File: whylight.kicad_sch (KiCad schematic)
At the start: 69 parts, among them J1 USB device, J2 External 5v, J3 External 5v, J4 I2C, J5 UART, J7 Ledstrip, U1 AG5405, U10 INA233, U11 L78L05_SOT89, U2 KPC357NT0ATLD, U3 ESP32-C6-WROOM-1, U4 Ra-01SH, U6 AP63203WU, U7 USBLC6-2P6, U8 74LVC1G125, U9 74LVC1G125

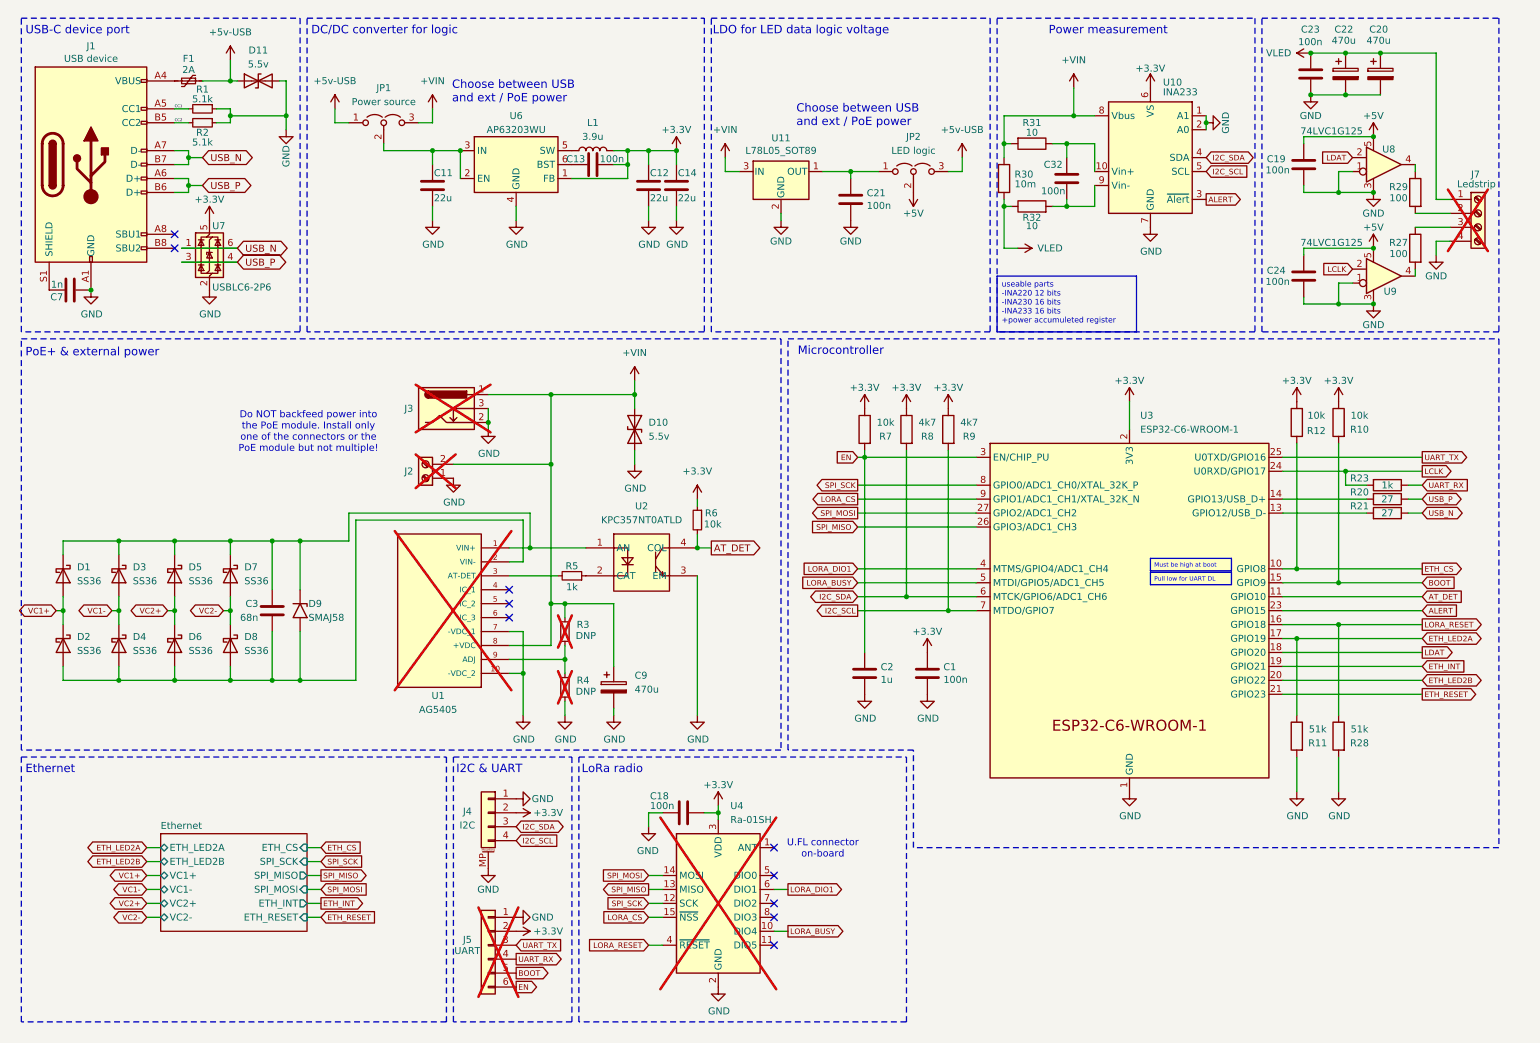
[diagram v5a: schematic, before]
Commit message: Add RS485, add mounting holes, route more stuff
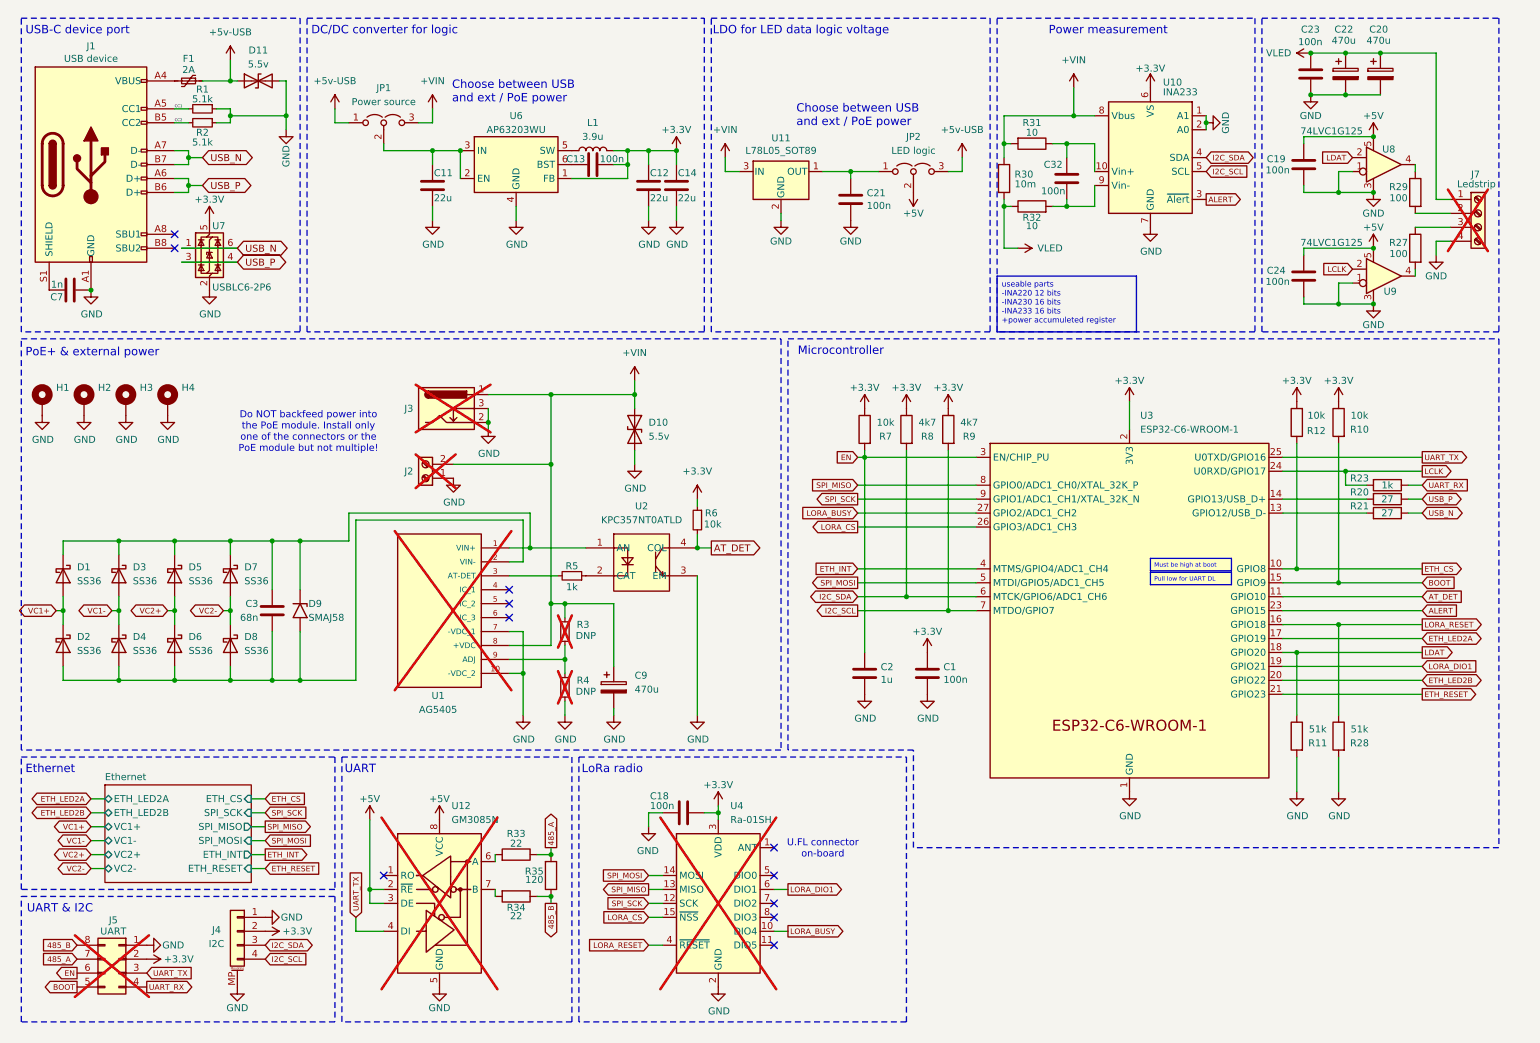
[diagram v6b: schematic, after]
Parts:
- added H1, H2, H3, H4: ~, MountingHole:MountingHole_2.2mm_M2, symbol Mechanical:MountingHole_Pad
- added R33, R34: 22, Resistor_SMD:R_0402_1005Metric, symbol symbols:R
- added R35: 120, Resistor_SMD:R_0402_1005Metric, symbol symbols:R
- added U12: GM3085N, Package_SO:SOIC-8_3.9x4.9mm_P1.27mm, symbol Interface_UART:SP3485EN
- J4: footprint Connector_JST:JST_SH_SM04B-SRSS-TB_1x04-1MP_P1.00mm_Horizontal -> Connector_JST:JST_SH_BM04B-SRSS-TB_1x04-1MP_P1.00mm_Vertical; LCSC C160404 -> (none)
- J5: footprint Connector_PinHeader_2.54mm:PinHeader_1x06_P2.54mm_Vertical -> Connector_PinHeader_2.54mm:PinHeader_2x04_P2.54mm_Vertical; symbol Connector_Generic:Conn_01x06 -> Connector_Generic:Conn_02x04_Counter_Clockwise; now in the parts list
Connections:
- net +5V: now also U12.2 (~{RE}), U12.3 (DE), U12.8 (VCC)
- net ETH_INT: now also U3.4 (MTMS/GPIO4/ADC1_CH4); no longer U3.19 (GPIO21)
- net ETH_LED2A: no longer R11.1
- net GND: now also H1.1, H2.1, H3.1, H4.1, U12.5 (GND)
- net LDAT: now also R11.1
- net LORA_BUSY: now also U3.27 (GPIO2/ADC1_CH2); no longer U3.5 (MTDI/GPIO5/ADC1_CH5)
- net LORA_CS: now also U3.26 (GPIO3/ADC1_CH3); no longer U3.9 (GPIO1/ADC1_CH1/XTAL_32K_N)
- net LORA_DIO1: now also U3.19 (GPIO21); no longer U3.4 (MTMS/GPIO4/ADC1_CH4)
- net SPI_MISO: now also U3.8 (GPIO0/ADC1_CH0/XTAL_32K_P); no longer U3.26 (GPIO3/ADC1_CH3)
- net SPI_MOSI: now also U3.5 (MTDI/GPIO5/ADC1_CH5); no longer U3.27 (GPIO2/ADC1_CH2)
- net SPI_SCK: now also U3.9 (GPIO1/ADC1_CH1/XTAL_32K_N); no longer U3.8 (GPIO0/ADC1_CH0/XTAL_32K_P)
- net UART_TX: now also U12.4 (DI)
- new net: R33.2, U12.6 (A)
- new net: R34.2, U12.7 (B)
- new net 485_A: J5.7 (Pin_7), R33.1, R35.2
- new net 485_B: J5.8 (Pin_8), R34.1, R35.1
- no-connect marks 10 -> 11
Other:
- note added: "UART"
- note added: "UART & I2C"
- note removed: "I2C & UART"
- moved on the sheet: J4

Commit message: Finish first pass of routing
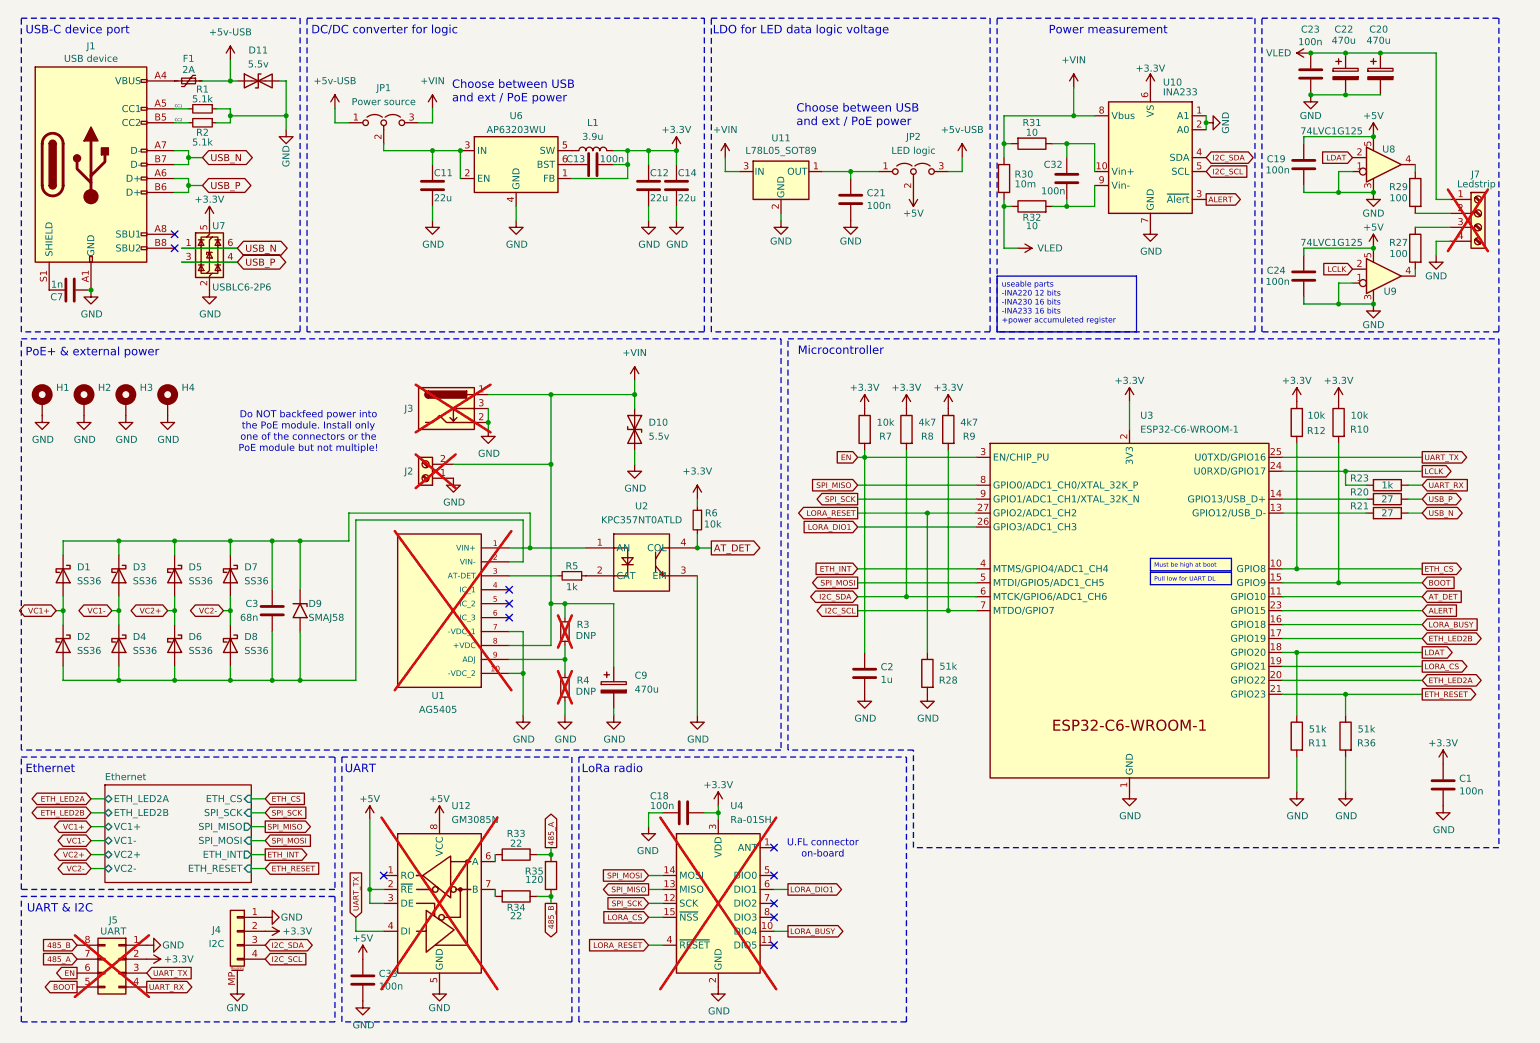
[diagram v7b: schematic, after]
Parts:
- added C33: 100n, Capacitor_SMD:C_0402_1005Metric, symbol symbols:C
- added R36: 51k, Resistor_SMD:R_0402_1005Metric, symbol symbols:R
- H1, H2, H3, H4: footprint MountingHole:MountingHole_2.2mm_M2 -> MountingHole:MountingHole_2.2mm_M2_DIN965_Pad
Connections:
- net +5V: now also C33.1
- net ETH_LED2A: now also U3.20 (GPIO22); no longer U3.17 (GPIO19)
- net ETH_LED2B: now also U3.17 (GPIO19); no longer U3.20 (GPIO22)
- net ETH_RESET: now also R36.1
- net GND: now also C33.2, R36.2
- net LORA_BUSY: now also U3.16 (GPIO18); no longer U3.27 (GPIO2/ADC1_CH2)
- net LORA_CS: now also U3.19 (GPIO21); no longer U3.26 (GPIO3/ADC1_CH3)
- net LORA_DIO1: now also U3.26 (GPIO3/ADC1_CH3); no longer U3.19 (GPIO21)
- net LORA_RESET: now also U3.27 (GPIO2/ADC1_CH2); no longer U3.16 (GPIO18)
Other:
- moved on the sheet: C1, R28

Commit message: r0.1
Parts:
- added N1: Logo, library:logo_nicolai, symbol Mechanical:Housing
- H1, H2, H3, H4: LCSC (none) -> -
- J4: LCSC (none) -> C160390
- R33, R34: LCSC (none) -> C25092
- R35: LCSC (none) -> C25079
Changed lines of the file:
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@@
 			)
 		)
-		(property "LCSC" ""
+		(property "LCSC" "C25092"
 			(at 104.14 166.37 0)
 			(effects
@@
 			)
 		)
-		(property "LCSC" ""
+		(property "LCSC" "C160390"
 			(at 53.34 180.34 0)
 			(effects
@@
 			)
 		)
-		(property "LCSC" ""
+		(property "LCSC" "C25092"
 			(at 104.14 173.99 0)
 			(effects
@@
 			)
 		)
+		(property "LCSC" "-"
+			(at 25.4 83.82 0)
+			(effects
+				(font
+					(size 1.27 1.27)
+				)
+				(hide yes)
+			)
+		)
 		(pin "1"
 		)
@@
 			)
 		)
+		(property "LCSC" "-"
+			(at 40.64 83.82 0)
+			(effects
+				(font
+					(size 1.27 1.27)
+				)
+				(hide yes)
+			)
+		)
 		(pin "1"
 		)
@@
 	)
 	(symbol
+		(lib_id "Mechanical:Housing")
+		(at 184.15 157.48 0)
+		(unit 1)
+		(exclude_from_sim yes)
+		(in_bom yes)
+		(on_board yes)
+		(dnp no)
+		(fields_autoplaced yes)
+		(property "Reference" "N1"
+			(at 187.96 156.5274 0)
+			(effects
+				(font
+					(size 1.27 1.27)
+				)
+				(justify left)
+			)
+		)
+		(property "Value" "Logo"
+			(at 187.96 159.0674 0)
+			(effects
+				(font
+					(size 1.27 1.27)
+				)
+				(justify left)
+			)
+		)
+		(property "Footprint" "library:logo_nicolai"
+			(at 185.42 156.21 0)
+			(effects
+				(font
+					(size 1.27 1.27)
+				)
+				(hide yes)
+			)
+		)
+		(property "Datasheet" ""
+			(at 185.42 156.21 0)
+			(effects
+				(font
+					(size 1.27 1.27)
+				)
+				(hide yes)
+			)
+		)
+		(property "Description" ""
+			(at 184.15 157.48 0)
+			(effects
+				(font
+					(size 1.27 1.27)
+				)
+				(hide yes)
+			)
+		)
+		(instances
+			(project ""
+				(path "/12ab2aee-f6e3-4178-94ff-8d6a84db0790"
+					(reference "N1")
+					(unit 1)
+				)
+			)
+		)
+	)
+	(symbol
 		(lib_id "Sensor_Energy:INA233")
 		(at 219.71 39.37 0)
@@
 			)
 		)
+		(property "LCSC" "-"
+			(at 33.02 83.82 0)
+			(effects
+				(font
+					(size 1.27 1.27)
+				)
+				(hide yes)
+			)
+		)
 		(pin "1"
 		)
@@
 			)
 		)
-		(property "LCSC" ""
+		(property "LCSC" "C25079"
 			(at 110.49 170.18 0)
 			(effects
@@
 			(at 17.78 83.82 0)
 			(effects
+				(font
+					(size 1.27 1.27)
+				)
+				(hide yes)
+			)
+		)
+		(property "LCSC" "-"
+			(at 17.78 83.82 0)
+			(effects
